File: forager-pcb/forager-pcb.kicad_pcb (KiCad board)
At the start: 2 copper layers, 272.5 x 96.3 mm, 102 parts, among them J1 Conn_01x02_Pin, J2 Conn_01x02_Pin

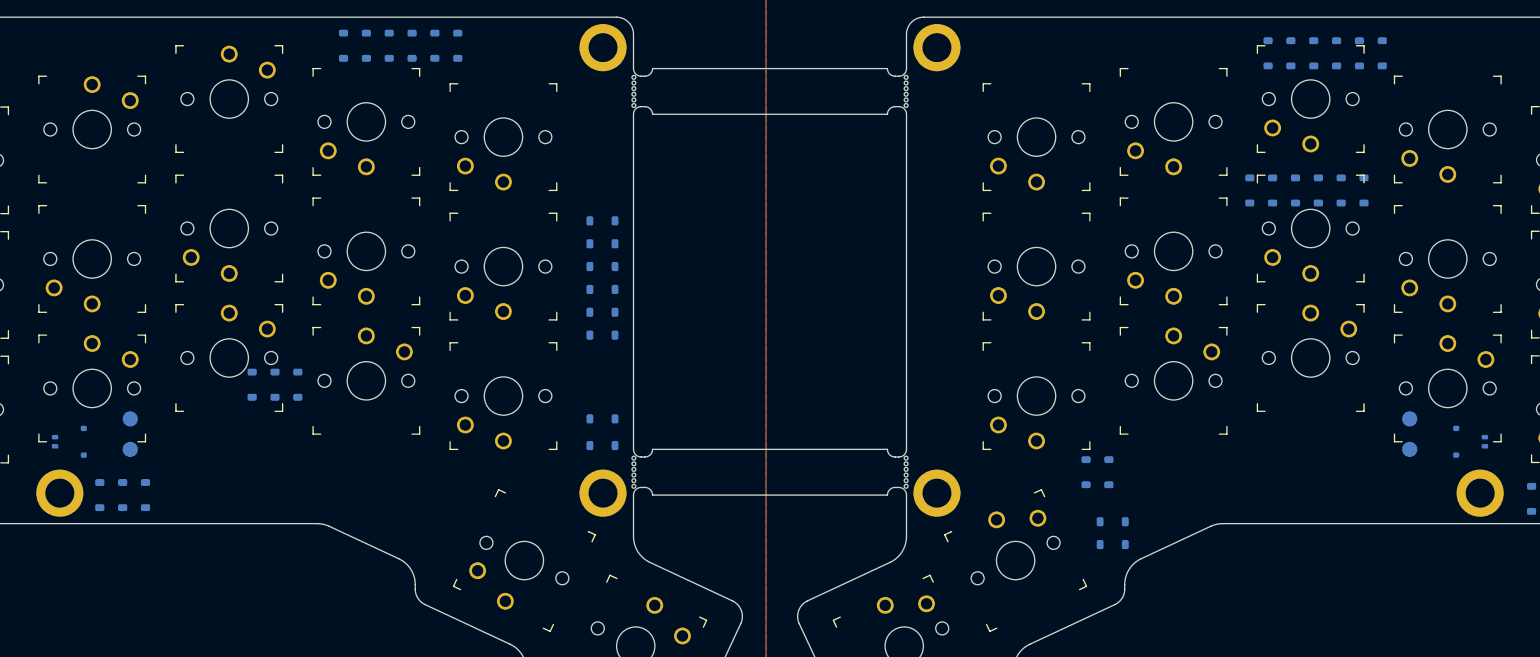
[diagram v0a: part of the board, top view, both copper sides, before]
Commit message: Align switches
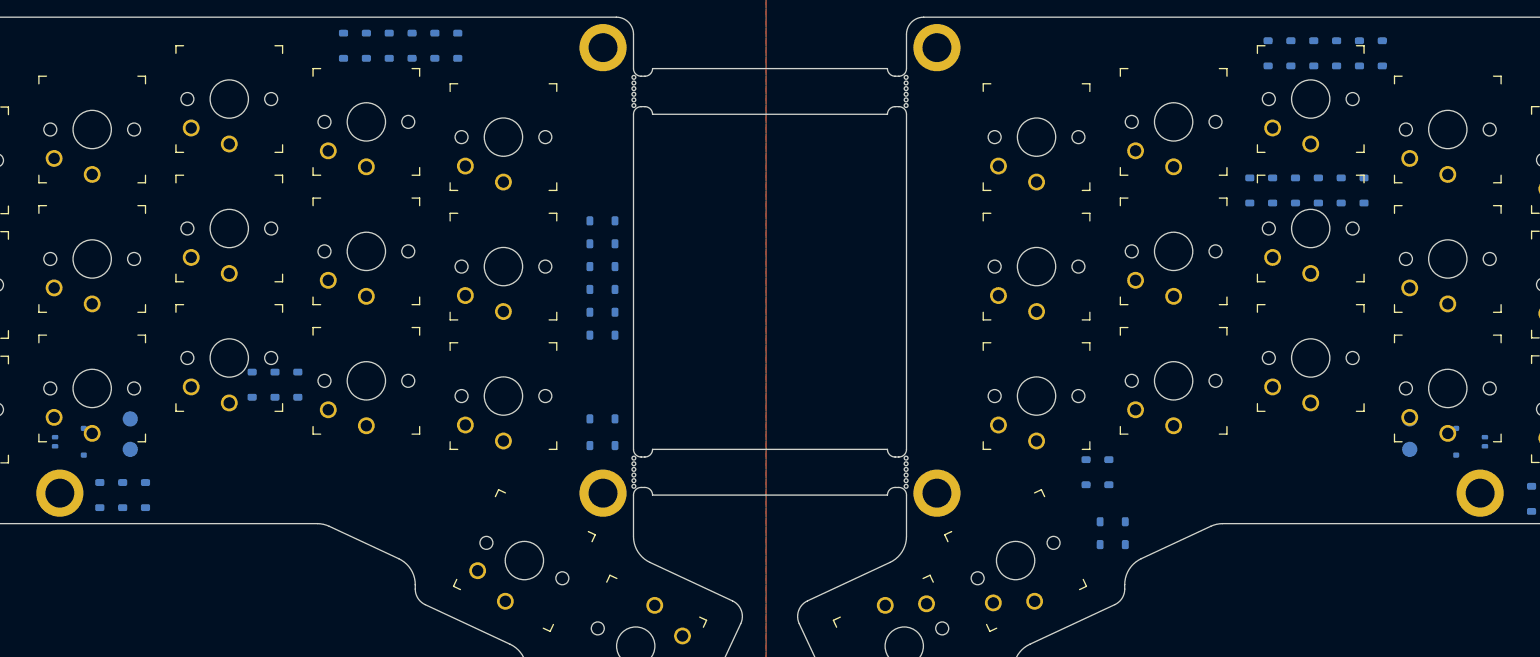
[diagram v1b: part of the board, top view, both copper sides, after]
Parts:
- turned LCH15 to 180 degrees
- turned LCH16 to 180 degrees
- turned LCH17 to 180 degrees
- turned LCH3 to 180 degrees
- turned LCH4 to 180 degrees
- turned RCH14 to 180 degrees
- turned RCH15 to 180 degrees
- turned RCH16 to 180 degrees
- turned RCH20 to -155 degrees

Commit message: Per switch diode
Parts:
- moved LD7 98.8 mm to (-119.5, -7.00), turned to 90 degrees
- moved LD8 80.1 mm to (-101.5, -10.5), turned to 90 degrees
- moved LD1 75.8 mm to (-119.5, -24.0), turned to 90 degrees
- moved LD9 61.6 mm to (-83.5, -14.0), turned to 90 degrees
- moved RD12 56.2 mm to (130.5, -7.00), turned to 90 degrees
- moved LD2 54.9 mm to (-101.5, -27.0), turned to 90 degrees
- moved RD6 54.3 mm to (130.5, -24.0), turned to 90 degrees
- moved LD10 43.7 mm to (-65.5, -18.0), turned to 90 degrees
- moved RD11 41.0 mm to (112.5, -10.5), turned to 90 degrees
- moved RD5 39.4 mm to (112.5, -27.0), turned to 90 degrees
- moved LD3 34.0 mm to (-83.5, -31.0), turned to 90 degrees
- moved LD18 33.0 mm to (-29.5, 4.00)
- moved LD13 31.6 mm to (-119.5, 10.0)
- moved RD1 29.1 mm to (40.5, -30.0), turned to 90 degrees
- moved LD20 28.0 mm to (-22.5, 34.5), turned to 90 degrees
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
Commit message: Internal switch routes
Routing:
- net Net-(LD20-A): track 0.00 -> 12.3 mm
- net Net-(LD15-A): track 0.00 -> 11.5 mm
- net Net-(RD16-A): track 0.00 -> 11.3 mm
- net Net-(RD8-A): track 0.00 -> 11.2 mm
- net Net-(RD2-A): track 0.00 -> 11.2 mm
- net Net-(RD14-A): track 0.00 -> 11.2 mm
- net Net-(LD18-A): track 0.00 -> 11.2 mm
- net Net-(RD18-A): track 0.00 -> 11.2 mm
- net Net-(RD15-A): track 0.00 -> 11.2 mm
- net Net-(RD12-A): track 0.00 -> 11.2 mm
- net Net-(RD10-A): track 0.00 -> 11.2 mm
- net Net-(RD6-A): track 0.00 -> 11.2 mm
- net Net-(RD5-A): track 0.00 -> 11.2 mm
- net Net-(RD4-A): track 0.00 -> 11.2 mm
- net Net-(RD20-A): track 0.00 -> 11.1 mm
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
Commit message: Cross switch diodes
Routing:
- net /LROW2: track 0.00 -> 108.1 mm
- net /RROW2: track 0.00 -> 104.7 mm
- net /RROW0: track 0.00 -> 101.1 mm
- net /RROW1: track 0.00 -> 100.9 mm
- net /LROW1: track 0.00 -> 99.5 mm
- net /LROW0: track 0.00 -> 99.5 mm
- net /RROW3: track 0.00 -> 20.1 mm
- net /LROW3: track 0.00 -> 11.1 mm

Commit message: Top cross switches
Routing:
- net /LCOL4: track 0.00 -> 71.9 mm
- net /RCOL4: track 0.00 -> 71.6 mm
- net /LCOL5: track 0.00 -> 70.4 mm
- net /RCOL5: track 0.00 -> 69.7 mm
- net /LCOL0: track 0.00 -> 39.3 mm
- net /RCOL0: track 0.00 -> 38.9 mm
- net /LCOL3: track 0.00 -> 38.7 mm
- net /RCOL3: track 0.00 -> 38.7 mm
- net /RCOL1: track 0.00 -> 38.7 mm
- net /LCOL1: track 0.00 -> 37.5 mm
- net /RCOL2: track 0.00 -> 24.6 mm
- net /LCOL2: track 0.00 -> 24.6 mm
- net LBAT: track 0.00 -> 10.9 mm
- net RBAT: track 0.00 -> 10.0 mm

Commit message: Top to controller
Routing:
- net /RCOL5: track 69.7 -> 167.0 mm, vias 0 -> 1
- net /LCOL5: track 70.4 -> 164.7 mm, vias 0 -> 1
- net /RCOL4: track 71.6 -> 150.7 mm, vias 0 -> 1
- net /LCOL4: track 71.9 -> 148.1 mm, vias 0 -> 1
- net /RCOL3: track 38.7 -> 99.6 mm, vias 0 -> 1
- net /LCOL3: track 38.7 -> 98.9 mm, vias 0 -> 1
- net /LCOL2: track 24.6 -> 71.6 mm, vias 0 -> 1
- net /RCOL2: track 24.6 -> 61.4 mm, vias 0 -> 1
- net /LCOL1: track 37.5 -> 72.3 mm, vias 0 -> 1
- net /LCOL0: track 39.3 -> 72.1 mm, vias 0 -> 1
- net /RCOL1: track 38.7 -> 65.5 mm, vias 0 -> 1
- net /RCOL0: track 38.9 -> 50.8 mm, vias 0 -> 1

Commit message: Connect power
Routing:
- net RBAT: track 10.0 -> 93.6 mm, vias 0 -> 1
- net LBAT: track 10.9 -> 82.0 mm, vias 0 -> 1
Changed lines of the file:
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@@
+	)
+	(segment
+		(start -99 -32.5)
+		(end -106.899 -40.399)
+		(width 0.4)
+		(layer "F.Cu")
+		(net 2)
+	)
+	(segment
+		(start -99 -2)
+		(end -99 -32.5)
+		(width 0.4)
+		(layer "F.Cu")
+		(net 2)
+	)
+	(segment
+		(start -120.869969 -40.399)
+		(end -125.055327 -44.584358)
+		(width 0.4)
+		(layer "F.Cu")
+		(net 2)
+	)
+	(segment
+		(start -95.5 1.5)
+		(end -99 -2)
+		(width 0.4)
+		(layer "F.Cu")
+		(net 2)
+	)
+	(segment
+		(start -106.899 -40.399)
+		(end -120.869969 -40.399)
+		(width 0.4)
+		(layer "F.Cu")
+		(net 2)
+	)
+	(via
+		(at -95.5 1.5)
+		(size 0.8)
+		(drill 0.4)
+		(layers "F.Cu" "B.Cu")
+		(net 2)
+	)
+	(segment
+		(start -93.875 3.125)
+		(end -95.5 1.5)
+		(width 0.4)
+		(layer "B.Cu")
+		(net 2)
 	)
 	(segment
@@
 		(start -86.4 5.4)
 		(end -84 3)
+		(width 0.4)
+		(layer "B.Cu")
+		(net 2)
+	)
+	(segment
+		(start -93.875 5.4)
+		(end -93.875 3.125)
 		(width 0.4)
 		(layer "B.Cu")
@@
 	)
 	(segment
+		(start -120.0671 -41)
+		(end -125.0671 -46)
+		(width 0.2)
+		(layer "F.Cu")
+		(net 7)
+	)
+	(segment
+		(start -96.7019 -33.7019)
+		(end -104 -41)
+		(width 0.2)
+		(layer "F.Cu")
+		(net 7)
+	)
+	(segment
 		(start -104 -41)
-		(end -120.817072 -41)
+		(end -120.0671 -41)
+		(width 0.2)
+		(layer "F.Cu")
+		(net 7)
+	)
+	(segment
+		(start -91.8655 -26.2345)
+		(end -91.8655 -14.9655)
+		(width 0.2)
+		(layer "F.Cu")
+		(net 7)
+	)
+	(segment
+		(start -89 -29.1)
+		(end -91.8655 -26.2345)
 		(width 0.2)
 		(layer "F.Cu")
@@
 	)
 	(segment
-		(start -91.8655 -26.2345)
-		(end -91.8655 -14.9655)
-		(width 0.2)
-		(layer "F.Cu")
-		(net 7)
-	)
-	(segment
-		(start -125.817072 -46)
+		(start -125.0671 -46)
 		(end -127 -46)
-		(width 0.2)
-		(layer "F.Cu")
-		(net 7)
-	)
-	(segment
-		(start -89 -29.1)
-		(end -91.8655 -26.2345)
 		(width 0.2)
 		(layer "F.Cu")
@@
 	)
 	(segment
-		(start -96.7019 -33.7019)
-		(end -104 -41)
-		(width 0.2)
-		(layer "F.Cu")
-		(net 7)
-	)
-	(segment
 		(start -91.8655 -14.9655)
 		(end -89 -12.1)
-		(width 0.2)
-		(layer "F.Cu")
-		(net 7)
-	)
-	(segment
-		(start -120.817072 -41)
-		(end -125.817072 -46)
 		(width 0.2)
 		(layer "F.Cu")
@@
 	(segment
 		(start -90.186929 -32.1345)
+		(end -75.7655 -32.1345)
+		(width 0.2)
+		(layer "F.Cu")
+		(net 10)
+	)
+	(segment
+		(start -92 -35.5)
 		(end -92 -33.947571)
 		(width 0.2)
@@
 	)
 	(segment
-		(start -92 -33.947571)
-		(end -92 -35.5)
-		(width 0.2)
-		(layer "F.Cu")
-		(net 10)
-	)
-	(segment
-		(start -92 -35.5)
-		(end -98.047 -41.547)
-		(width 0.2)
-		(layer "F.Cu")
-		(net 10)
-	)
-	(segment
 		(start -73.8655 -30.2345)
 		(end -73.8655 -18.9655)
@@
 	)
 	(segment
+		(start -75.7655 -32.1345)
+		(end -73.8655 -30.2345)
+		(width 0.2)
+		(layer "F.Cu")
+		(net 10)
+	)
+	(segment
 		(start -73.8655 -18.9655)
 		(end -71 -16.1)
@@
 	)
 	(segment
-		(start -120.047 -41.547)
-		(end -124.5 -46)
+		(start -119.047 -41.547)
+		(end -98.047 -41.547)
+		(width 0.2)
+		(layer "F.Cu")
+		(net 10)
+	)
+	(segment
+		(start -124 -46.5)
+		(end -119.047 -41.547)
 		(width 0.2)
 		(layer "F.Cu")
@@
 	)
 	(segment
-		(start -75.7655 -32.1345)
+		(start -92 -33.947571)
 		(end -90.186929 -32.1345)
-		(width 0.2)
-		(layer "F.Cu")
-		(net 10)
-	)
-	(segment
-		(start -98.047 -41.547)
-		(end -120.047 -41.547)
-		(width 0.2)
-		(layer "F.Cu")
-		(net 10)
-	)
-	(segment
-		(start -73.8655 -30.2345)
-		(end -75.7655 -32.1345)
 		(width 0.2)
 		(layer "F.Cu")
@@
 		(net 10)
 	)
+	(segment
+		(start -98.047 -41.547)
+		(end -92 -35.5)
+		(width 0.2)
+		(layer "F.Cu")
+		(net 10)
+	)
 	(via
-		(at -124.5 -46)
+		(at -124 -46.5)
 		(size 0.6)
 		(drill 0.3)
@@
 	)
 	(segment
+		(start -124 -46.5)
+		(end -125 -46.5)
+		(width 0.2)
+		(layer "B.Cu")
+		(net 10)
+	)
+	(segment
 		(start -125.5 -47)
-		(end -124.5 -46)
-		(width 0.2)
-		(layer "B.Cu")
-		(net 10)
-	)
-	(segment
-		(start -125.5 -47.62)
+		(end -125.5 -47.62)
+		(width 0.2)
+		(layer "B.Cu")
+		(net 10)
+	)
+	(segment
+		(start -125 -46.5)
 		(end -125.5 -47)
 		(width 0.2)
@@
 	)
 	(segment
+		(start 80.5 -22.872642)
+		(end 89.661858 -32.0345)
+		(width 0.4)
+		(layer "F.Cu")
+		(net 32)
+	)
+	(segment
+		(start 100.5 -34.5)
+		(end 114.5 -34.5)
+		(width 0.4)
+		(layer "F.Cu")
+		(net 32)
+	)
+	(segment
+		(start 122.262 -32)
+		(end 125.517375 -35.255375)
+		(width 0.4)
+		(layer "F.Cu")
+		(net 32)
+	)
+	(segment
+		(start 89.661858 -32.0345)
+		(end 98.0345 -32.0345)
+		(width 0.4)
+		(layer "F.Cu")
+		(net 32)
+	)
+	(segment
+		(start 114.5 -34.5)
+		(end 117 -32)
+		(width 0.4)
+		(layer "F.Cu")
+		(net 32)
+	)
+	(segment
+		(start 80.5 2.5)
+		(end 80.5 -22.872642)
+		(width 0.4)
+		(layer "F.Cu")
+		(net 32)
+	)
+	(segment
+		(start 117 -32)
+		(end 122.262 -32)
+		(width 0.4)
+		(layer "F.Cu")
+		(net 32)
+	)
+	(segment
+		(start 98.0345 -32.0345)
+		(end 100.5 -34.5)
+		(width 0.4)
+		(layer "F.Cu")
+		(net 32)
+	)
+	(via
+		(at 80.5 2.5)
+		(size 0.8)
+		(drill 0.4)
+		(layers "F.Cu" "B.Cu")
+		(net 32)
+	)
+	(segment
 		(start 84.4 6.6)
 		(end 93.875 6.6)
 		(width 0.4)
 		(layer "B.Cu")
+		(net 32)
+	)
+	(segment
+		(start 80.5 3.5)
+		(end 80.5 2.5)
+		(width 0.4)
+		(layer "B.Cu")
+		(net 32)
+	)
+	(segment
+		(start 84 7)
+		(end 80.5 3.5)
+		(width 0.4)
+		(layer "B.Cu")

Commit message: Connect remaining to controller
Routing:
- net /LROW3: track 11.1 -> 186.1 mm
- net /RROW3: track 20.1 -> 169.8 mm
- net /RROW2: track 104.7 -> 151.6 mm
- net /RROW1: track 100.9 -> 146.2 mm, vias 0 -> 2
- net /LROW2: track 108.1 -> 153.4 mm, vias 0 -> 2
- net /LROW0: track 99.5 -> 136.0 mm
- net /LROW1: track 99.5 -> 130.5 mm, vias 0 -> 2
- net /RROW0: track 101.1 -> 127.1 mm
- net LGND: track 0.00 -> 2.27 mm, vias 0 -> 11
- net RGND: track 0.00 -> 2.20 mm, vias 0 -> 9
- net /RCOL2: track 61.4 -> 60.3 mm
- net /RCOL1: track 65.5 -> 64.5 mm
